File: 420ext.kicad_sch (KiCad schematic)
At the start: 5 parts, among them J35 PT

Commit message: Added LC filter for power filtering
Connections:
- net at R106.2: now also J35.2 (Pin_2); no longer J35.3 (Pin_3)
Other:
- moved on the sheet: C61, R106, R107, U34

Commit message: Updates after PDR
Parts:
- added C81: ?, Capacitor_SMD:C_0402_1005Metric, symbol Device:C_Small
- added C84: 100nF, Capacitor_SMD:C_0402_1005Metric, symbol Device:C_Small
- added D38: BZT52C3V3LP-7, Diode_SMD:D_0402_1005Metric_Pad0.77x0.64mm_HandSolder, symbol UCIRP-KiCAD-Lib:D_Zener_Small
- added R127: 0R, Resistor_SMD:R_0402_1005Metric, symbol Device:R_Small_US
- added U51: ~, Package_TO_SOT_SMD:SOT-23-5, symbol UCIRP-KiCAD-Lib:MCP6001
- J35: value PT -> 420Sensor
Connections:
- net +3.3V: now also C84.1, U51.5 (V+)
- net GND: now also C81.2, C84.2, D38.2 (A), U51.2 (V-)
- net OUT: now also U51.1, U51.4 (-); no longer U34.1, U34.4 (-)
- net at R106.1, R107.2, U34.3 (+): now also D38.1 (K)
- new net: R127.2, U34.1, U34.4 (-)
- new net: C81.1, R127.1, U51.3 (+)
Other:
- note added: "Configurable low pass filter"
- note added: "Zener diode caps voltage at 3.3V"
- note removed: "500Ω resistor is to ensure that shorts wont damage the sensing circuitry."
- moved on the sheet: R107, U34

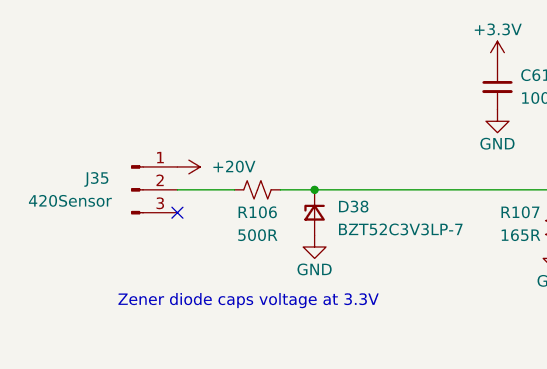
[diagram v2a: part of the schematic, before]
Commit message: Updated to add beginnings of layout. Most major subsystems internally layed out
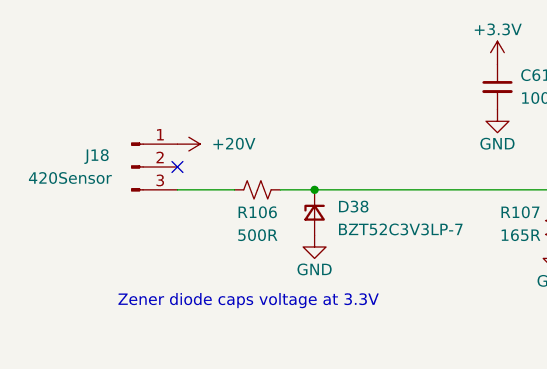
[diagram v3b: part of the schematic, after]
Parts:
- removed J35: 420Sensor, 0UCIRP-KiCAD-Lib:GX-12 3 pin, symbol Connector:Conn_01x03_Pin
- added J18: 420Sensor, 0UCIRP-KiCAD-Lib:GX-12 3 pin, symbol Connector:Conn_01x03_Pin
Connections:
- net +20V: now also J18.1 (Pin_1)
- net at R106.2: now also J18.3 (Pin_3)
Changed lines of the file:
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@@
 	)
 	(no_connect
-		(at 109.22 96.52)
+		(at 109.22 91.44)
 	)
 	(wire
@@
 	(symbol
 		(lib_id "power:+24V")
-		(at 109.22 91.44 270)
+		(at 109.22 88.9 270)
 		(unit 1)
 		(exclude_from_sim no)
@@
 		(fields_autoplaced yes)
 		(property "Reference" "#PWR0282"
-			(at 105.41 91.44 0)
+			(at 105.41 88.9 0)
 			(effects
 				(font
@@
 		)
 		(property "Value" "+20V"
-			(at 113.03 91.44 90)
+			(at 113.03 88.9 90)
 			(effects
 				(font
@@
 		)
 		(property "Footprint" ""
-			(at 109.22 91.44 0)
+			(at 109.22 88.9 0)
 			(effects
 				(font
@@
 		)
 		(property "Datasheet" ""
-			(at 109.22 91.44 0)
+			(at 109.22 88.9 0)
 			(effects
 				(font
@@
 		)
 		(property "Description" ""
-			(at 109.22 91.44 0)
+			(at 109.22 88.9 0)
 			(effects
 				(font
@@
 	)
 	(symbol
+		(lib_id "Connector:Conn_01x03_Pin")
+		(at 104.14 91.44 0)
+		(unit 1)
+		(exclude_from_sim no)
+		(in_bom yes)
+		(on_board yes)
+		(dnp no)
+		(property "Reference" "J18"
+			(at 100.33 90.17 0)
+			(effects
+				(font
+					(size 1.27 1.27)
+				)
+			)
+		)
+		(property "Value" "420Sensor"
+			(at 97.282 92.71 0)
+			(effects
+				(font
+					(size 1.27 1.27)
+				)
+			)
+		)
+		(property "Footprint" "0UCIRP-KiCAD-Lib:GX-12 3 pin"
+			(at 104.14 91.44 0)
+			(effects
+				(font
+					(size 1.27 1.27)
+				)
+				(hide yes)
+			)
+		)
+		(property "Datasheet" "~"
+			(at 104.14 91.44 0)
+			(effects
+				(font
+					(size 1.27 1.27)
+				)
+				(hide yes)
+			)
+		)
+		(property "Description" ""
+			(at 104.14 91.44 0)
+			(effects
+				(font
+					(size 1.27 1.27)
+				)
+			)
+		)
+		(property "Manufacturer" "~"
+			(at 104.14 91.44 0)
+			(effects
+				(font
+					(size 1.27 1.27)
+				)
+				(hide yes)
+			)
+		)
+		(property "Part #" "~"
+			(at 104.14 91.44 0)
+			(effects
+				(font
+					(size 1.27 1.27)
+				)
+				(hide yes)
+			)
+		)
+		(pin "1"
+		)
+		(pin "2"
+		)
+		(pin "3"
+		)
+		(instances
+			(project "gse2-hardware"
+				(path "/1eb2a3ff-e0fd-4343-8dba-716780a4d459/5559a045-5274-46dd-a9f7-6c77421fac55"
+					(reference "J18")
+					(unit 1)
+				)
+				(path "/1eb2a3ff-e0fd-4343-8dba-716780a4d459/b9e77221-eaa0-4bf3-ad88-5995c45b6f4d"
+					(reference "J31")
+					(unit 1)
+				)
+				(path "/1eb2a3ff-e0fd-4343-8dba-716780a4d459/f58ffc9d-63e0-47ae-abea-627da656b710"
+					(reference "J30")
+					(unit 1)
+				)
+			)
+		)
+	)
+	(symbol
 		(lib_id "power:+5V")
 		(at 165.1 86.36 0)
@@
 					(unit 1)
 				)
-			)
-		)
-	)
-	(symbol
-		(lib_id "Connector:Conn_01x03_Pin")
-		(at 104.14 93.98 0)
-		(unit 1)
-		(exclude_from_sim no)
-		(in_bom yes)
-		(on_board yes)
-		(dnp no)
-		(property "Reference" "J35"
-			(at 100.33 92.71 0)
-			(effects
-				(font
-					(size 1.27 1.27)
-				)
-			)
-		)
-		(property "Value" "420Sensor"
-			(at 97.282 95.25 0)
-			(effects
-				(font
-					(size 1.27 1.27)
-				)
-			)
-		)
-		(property "Footprint" "0UCIRP-KiCAD-Lib:GX-12 3 pin"
-			(at 104.14 93.98 0)
-			(effects
-				(font
-					(size 1.27 1.27)
-				)
-				(hide yes)
-			)
-		)
-		(property "Datasheet" "~"
-			(at 104.14 93.98 0)
-			(effects
-				(font
-					(size 1.27 1.27)
-				)
-				(hide yes)
-			)
-		)
-		(property "Description" ""
-			(at 104.14 93.98 0)
-			(effects
-				(font
-					(size 1.27 1.27)
-				)
-			)
-		)
-		(property "Manufacturer" "~"
-			(at 104.14 93.98 0)
-			(effects
-				(font
-					(size 1.27 1.27)
-				)
-				(hide yes)
-			)
-		)
-		(property "Part #" "~"
-			(at 104.14 93.98 0)
-			(effects
-				(font
-					(size 1.27 1.27)
-				)
-				(hide yes)
-			)
-		)
-		(pin "1"
-		)
-		(pin "2"
-		)
-		(pin "3"
-		)
-		(instances
-			(project "gse2-hardware"
-				(path "/1eb2a3ff-e0fd-4343-8dba-716780a4d459/5559a045-5274-46dd-a9f7-6c77421fac55"
-					(reference "J35")
-					(unit 1)
-				)
-				(path "/1eb2a3ff-e0fd-4343-8dba-716780a4d459/b9e77221-eaa0-4bf3-ad88-5995c45b6f4d"
-					(reference "J31")
-					(unit 1)
-				)
-				(path "/1eb2a3ff-e0fd-4343-8dba-716780a4d459/f58ffc9d-63e0-47ae-abea-627da656b710"
-					(reference "J30")
-					(unit 1)
-				)
